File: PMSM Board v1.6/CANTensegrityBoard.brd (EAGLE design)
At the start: 100.5 x 48 mm, 94 parts, among them U1 REG711-5_DGK_8, U10 H1206T500R-10, U11 MH1608-600Y, U12 MH1608-600Y, U13 MH1608-600Y, U14 MH1608-600Y, U15 MH1608-600Y, U2 SN65HVD232_D_8, U3 SN65LVDT348_PW_1

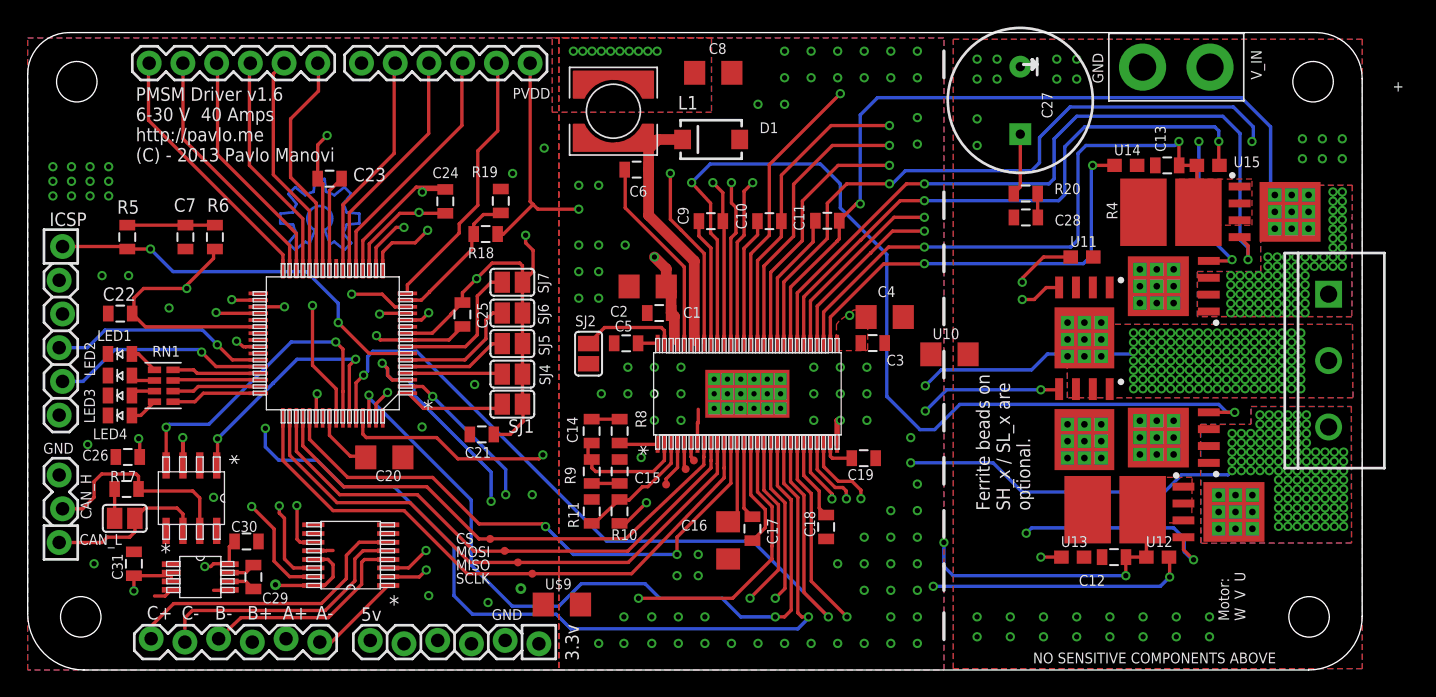
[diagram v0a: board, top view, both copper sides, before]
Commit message: Removed thermals in a few places.
Signed-off-by: Pavlo Manovi <pavlo.manovi@gmail.com>
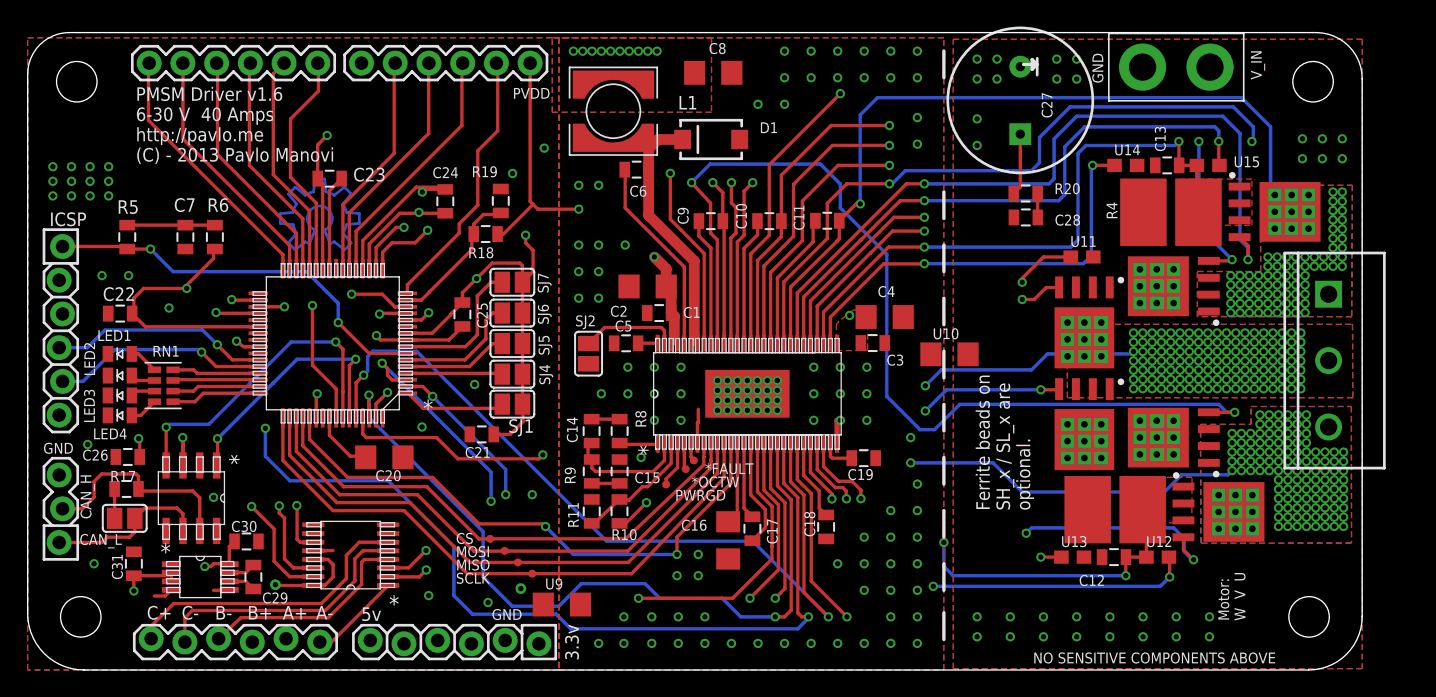
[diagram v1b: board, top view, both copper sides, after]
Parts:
- renumbered U$9 to U9
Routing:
- net CRNT2: track 72.4 -> 73.1 mm
- net PWM1L: track 55.5 -> 54.9 mm
- net DRV_GND: vias 80 -> 108
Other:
- board text added: "*FAULT"
- board text added: "*OCTW"
- board text added: "PWRGD"
- board text removed: "+"

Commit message: Generated gerbers and moved a power trace.
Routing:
- net GL_B: track 46.5 -> 45.4 mm
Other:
- board text added: "MCLR"
- board text added: "PMSM Driver v1.6 6-40 V 40 Amps http://pavlo.me (C) - 2013 Pavlo Manovi"
- board text removed: "PMSM Driver v1.6 6-30 V 40 Amps http://pavlo.me (C) - 2013 Pavlo Manovi"
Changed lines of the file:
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@@
 <?xml version="1.0" encoding="utf-8"?>
 <!DOCTYPE eagle SYSTEM "eagle.dtd">
-<eagle version="6.4">
+<eagle version="6.5.0">
 <drawing>
 <settings>
@@
 <text x="91.7" y="3.7" size="0.8128" layer="25" rot="R90">Motor:
 W  V  U</text>
-<text x="4.44" y="34.45" size="1.016" layer="25" rot="R180">ICSP</text>
+<text x="3.94" y="34.7" size="1.016" layer="25" rot="R180">ICSP</text>
 <text x="4.8" y="11.36" size="0.8128" layer="25" rot="R90">CAN_H</text>
 <text x="3.9" y="9.42" size="0.8128" layer="25">CAN_L</text>
@@
 <text x="81" y="44.17" size="0.8128" layer="25" rot="R90">GND</text>
 <text x="8.14" y="38.29" size="1.016" layer="25" font="vector">PMSM Driver v1.6
-6-30 V  40 Amps
+6-40 V  40 Amps
 http://pavlo.me
 (C) - 2013 Pavlo Manovi</text>
@@
 <text x="50" y="13.75" size="0.8128" layer="25">*OCTW</text>
 <text x="48.75" y="12.75" size="0.8128" layer="25">PWRGD</text>
+<text x="4.05" y="33.44" size="1.016" layer="25" rot="R270">MCLR</text>
 </plain>
 <attributes>
@@
 </element>
 <element name="SJ4" library="jumper" package="SJ" value="" x="36.5" y="22.28" smashed="yes" rot="R180">
-<attribute name="NAME" x="38.543" y="23.021" size="0.8128" layer="25" ratio="10" rot="R270"/>
 <attribute name="VALUE" x="36.0999" y="22.28" size="0.02" layer="27" rot="R180"/>
 </element>
 <element name="SJ5" library="jumper" package="SJ" value="" x="36.5" y="24.58" smashed="yes" rot="R180">
-<attribute name="NAME" x="38.483" y="25.251" size="0.8128" layer="25" ratio="10" rot="R270"/>
 <attribute name="VALUE" x="36.0999" y="24.58" size="0.02" layer="27" rot="R180"/>
 </element>
 <element name="SJ6" library="jumper" package="SJ" value="" x="36.5" y="26.88" smashed="yes" rot="R180">
-<attribute name="NAME" x="38.433" y="27.571" size="0.8128" layer="25" ratio="10" rot="R270"/>
 <attribute name="VALUE" x="36.0999" y="26.88" size="0.02" layer="27" rot="R180"/>
 </element>
 <element name="SJ7" library="jumper" package="SJ" value="" x="36.5" y="29.2" smashed="yes" rot="R180">
-<attribute name="NAME" x="38.423" y="29.931" size="0.8128" layer="25" ratio="10" rot="R270"/>
 <attribute name="VALUE" x="36.0999" y="29.2" size="0.02" layer="27" rot="R180"/>
 </element>
@@
 </element>
 <element name="SJ1" library="jumper" package="SJ" value="" x="36.5" y="20.02" smashed="yes" rot="R180">
-<attribute name="NAME" x="38.151" y="18.877" size="1.016" layer="25" ratio="10" rot="R180"/>
 <attribute name="VALUE" x="36.0999" y="20.02" size="0.02" layer="27" rot="R180"/>
 </element>
@@
 </element>
 <element name="U12" library="pavlo" package="0603" value="MH1608-600Y" x="85.1" y="8.5" smashed="yes">
-<attribute name="NAME" x="84.211" y="9.262" size="0.8128" layer="25" font="vector"/>
+<attribute name="NAME" x="84.738" y="5.211" size="0.8128" layer="25" font="vector" rot="R90"/>
 <attribute name="VALUE" x="84.084" y="7.357" size="0.4064" layer="27" font="vector"/>
 </element>
 <element name="U13" library="pavlo" package="0603" value="MH1608-600Y" x="78.7" y="8.5" smashed="yes">
-<attribute name="NAME" x="77.811" y="9.262" size="0.8128" layer="25" font="vector"/>
+<attribute name="NAME" x="78.488" y="5.311" size="0.8128" layer="25" font="vector" rot="R90"/>
 <attribute name="VALUE" x="77.684" y="7.357" size="0.4064" layer="27" font="vector"/>
 </element>
 <element name="U14" library="pavlo" package="0603" value="MH1608-600Y" x="82.7" y="38" smashed="yes">
-<attribute name="NAME" x="81.811" y="38.762" size="0.8128" layer="25" font="vector"/>
+<attribute name="NAME" x="81.811" y="39.262" size="0.8128" layer="25" font="vector"/>
 <attribute name="VALUE" x="81.684" y="36.857" size="0.4064" layer="27" font="vector"/>
 </element>
 <element name="U15" library="pavlo" package="0603" value="MH1608-600Y" x="88.9" y="38" smashed="yes">
-<attribute name="NAME" x="90.811" y="37.862" size="0.8128" layer="25" font="vector"/>
+<attribute name="NAME" x="91.061" y="37.862" size="0.8128" layer="25" font="vector"/>
 <attribute name="VALUE" x="87.884" y="36.857" size="0.4064" layer="27" font="vector"/>
 </element>
@@
 <wire x1="60.6" y1="39.5" x2="64.9" y2="39.5" width="0.254" layer="1"/>
 <via x="64.9" y="39.5" extent="1-16" drill="0.4" shape="square"/>
-<wire x1="64.9" y1="39.5" x2="64.6" y2="39.5" width="0.254" layer="15"/>
-<wire x1="64.6" y1="39.5" x2="63.8" y2="38.7" width="0.254" layer="15"/>
-<wire x1="63.8" y1="38.7" x2="63.8" y2="36.1" width="0.254" layer="15"/>
-<wire x1="63.8" y1="36.1" x2="64.5" y2="35.4" width="0.254" layer="15"/>
-<wire x1="64.5" y1="35.4" x2="64.5" y2="29.4" width="0.254" layer="15"/>
-<wire x1="64.5" y1="29.4" x2="66" y2="27.9" width="0.254" layer="15"/>
-<wire x1="66" y1="27.9" x2="74.9" y2="27.9" width="0.254" layer="15"/>
 <via x="74.9" y="27.9" extent="1-16" drill="0.4" shape="square"/>
 <wire x1="74.9" y1="27.9" x2="75.8" y2="27.9" width="0.254" layer="1"/>
@@
 <wire x1="77.665" y1="28.8" x2="77.675" y2="28.81" width="0.254" layer="1"/>
 <contactref element="U$2" pad="40"/>
+<wire x1="64.9" y1="39.5" x2="64.5" y2="39.5" width="0.254" layer="16"/>
+<wire x1="64.5" y1="39.5" x2="63.75" y2="38.75" width="0.254" layer="16"/>
+<wire x1="63.75" y1="38.75" x2="63.75" y2="35" width="0.254" layer="16"/>
+<wire x1="63.75" y1="35" x2="66" y2="32.75" width="0.254" layer="16"/>
+<wire x1="66" y1="32.75" x2="66" y2="30" width="0.254" layer="16"/>
+<wire x1="66" y1="30" x2="68" y2="28" width="0.254" layer="16"/>
+<wire x1="68" y1="28" x2="74.8" y2="28" width="0.254" layer="16"/>
+<wire x1="74.8" y1="28" x2="74.9" y2="27.9" width="0.254" layer="16"/>
 </signal>
 <signal name="GH_C">

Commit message: 1.7 Progress
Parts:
- removed C14: 120pF 5%, ASL:0805
- removed C15: 6.8nF 10%, ASL:0805
- removed C29: .22uF, ASL:0805
- removed C30, C31: 2.2uF, ASL:0805
- removed C5: .015 uF 60V 10%, ASL:0805
- removed C6: .1 uF 60V, ASL:0805
- removed C8: 47uF 16V, ASL:1206
- removed D1: DIODE-SCHOTTKY_, ASL:SMA-DIODE
- removed L1: 22 uH - MSS6132-223MLB, pavlo:MSS6132
- removed R10: 31.6 k 1%, ASL:0805
- removed R11: 10 k 1%, ASL:0805
- removed R8: 205 k 1%, ASL:0805
- removed R9: 16.2 k, ASL:0805
- removed SJ2: (no value), jumper:SJ
- removed TP5: TPTP06R, testpad:TP06R
- removed U1: REG711-5_DGK_8, pavlo:DGK8
- removed U11, U12, U13, U14, U15: MH1608-600Y, pavlo:0603
- added IC1: DRV8303, OpenPMSM:HTSSOP-480-DCA
- added R1: (no value), ASL:0805
- added U$10, U$11, U$12, U$9: NETJUMPER, OpenPMSM:NETJUMPER
- U$2: value DRV8301 -> NETJUMPER; device pavlo:DCA56_6P35X3P61 -> OpenPMSM:NETJUMPER
- moved U$2 26.1 mm to (77.2, 8.55), turned to 0 degrees
- moved TP7 1.83 mm to (48.5, 15.2)
- moved TP6 1.54 mm to (48.4, 16.2)
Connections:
- removed net N$10: C11.1, U$2.38
- removed net N$13: C29.2, U1.6
- removed net N$14: R8.1, U$2.1
- removed net N$15: C15.2, R9.2
- removed net N$16: C14.2, R9.1, U$2.2
- removed net N$17: R10.1, R11.2, U$2.3
- removed net N$23: C29.1, U1.7
- removed net N$7: TP5.TP, U$2.4
- removed net N$8: C9.1, U$2.48
- removed net N$9: C10.1, U$2.43
- removed net PH1: C6.2, D1.C, L1.P$1, U$2.50, U$2.51
- new net BST_B: C10.1, IC1.39
- new net BST_C: C11.1, IC1.34
- net *SCS: now also IC1.4; no longer U$2.8
- net CRNT1: now also IC1.21; no longer U$2.25
- net CRNT2: now also IC1.22; no longer U$2.26
- net DC_CAL: now also IC1.8; no longer U$2.12
- net DRV_GND: now also IC1.24, IC1.46, IC1.47, IC1.48, IC1.49, R1.1; no longer C14.1, C15.1, C5.2, C8.2, D1.A, R11.1, R8.2, SJ2.2, U$2.28, U$2.57, U$2.7
- net EN_GATE: now also IC1.12; no longer U$2.16
- net GH_A: now also IC1.43; no longer U$2.47
- net GH_B: now also IC1.38; no longer U$2.42
- net GH_C: now also IC1.33; no longer U$2.37
- net GL_A: now also IC1.41; no longer U$2.45
- net GL_B: now also IC1.36; no longer U$2.40
- net GL_C: now also IC1.31; no longer U$2.35
- net GND: no longer C30.1, C31.2, U1.4, U1.5
- net MISO: now also IC1.6; no longer U$2.10
- net MOSI: now also IC1.5; no longer U$2.9
- net N$1: now also IC1.3, R1.2; no longer C5.1, U$2.56
- net N$11: now also C9.2, IC1.42; no longer SJ2.1, U$2.55
- net N$12: now also IC1.1; no longer U$2.5
- net N$18: now also IC1.9; no longer U$2.13
- net N$19: now also IC1.10; no longer U$2.14
- net N$20: now also IC1.11; no longer U$2.15
- net N$21: now also IC1.19; no longer U$2.23
- net N$22: now also IC1.23; no longer U$2.27
- net N$24: now also IC1.2; no longer U$2.6
- net N$4: now also C9.1, IC1.44; no longer C6.1, U$2.52
- net PGND: now also U$10.P$2, U$11.P$2, U$2.P$2; no longer U11.2, U13.2, U14.2
- net PVDD: now also IC1.25; no longer U$2.29, U$2.53, U$2.54
- net PWM1H: now also IC1.13; no longer U$2.17
- net PWM1L: now also IC1.14; no longer U$2.18
- net PWM2H: now also IC1.15; no longer U$2.19
- net PWM2L: now also IC1.16; no longer U$2.20
- net PWM3H: now also IC1.17; no longer U$2.21
- net PWM3L: now also IC1.18; no longer U$2.22
- net SCLK: now also IC1.7; no longer U$2.11
- net SH_A: no longer C9.2, U$2.46
- net SH_B: now also IC1.37; no longer U$2.41
- net SH_C: now also IC1.32; no longer U$2.36
- net SL_A: now also IC1.40, U$9.P$2; no longer U$2.44, U12.2
- net SL_B: now also IC1.35, U$10.P$1; no longer U$2.39, U11.1
- net SL_C: now also IC1.30, U$12.P$2; no longer U$2.34, U15.2
- net SN1: now also IC1.29, U$9.P$1; no longer U$2.33, U12.1
- net SN2: now also IC1.27, U$12.P$1; no longer U$2.31, U15.1
- net SP1: now also IC1.28, U$2.P$1; no longer U$2.32, U13.1
- net SP2: now also IC1.26, U$11.P$1; no longer U$2.30, U14.1
- net VCC3V3: now also IC1.20, IC1.45; no longer C31.1, C8.1, L1.P$2, R10.2, U$2.24, U$2.49, U1.2, U1.3
- net VCC5V: no longer C30.2, U1.8
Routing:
- net SH_A: track 68.4 -> 0.00 mm, vias 119 -> 116
- net VCC3V3: track 149.1 -> 89.2 mm, vias 23 -> 19
- net PVDD: track 38.6 -> 87.4 mm
- net PH1: track 22.4 -> 0.00 mm
- net VCC5V: track 20.1 -> 0.00 mm, vias 1 -> 0
- net SH_B: track 63.4 -> 49.4 mm, vias 135 -> 134
- net N$10: track 10.5 -> 0.00 mm
- net BST_C: track 0.00 -> 10.5 mm
- net N$8: track 9.92 -> 0.00 mm
- net BST_B: track 0.00 -> 9.67 mm
- net N$9: track 9.62 -> 0.00 mm
- net N$17: track 9.25 -> 0.00 mm
- net N$16: track 9.23 -> 0.00 mm
- net DRV_GND: track 6.86 -> 0.63 mm, vias 108 -> 84
- net N$4: track 14.9 -> 9.63 mm
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- added copper zone on layer 15, net DRV_GND
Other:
- board text removed: "Ferrite beads on SH_x / SL_x are optional."
